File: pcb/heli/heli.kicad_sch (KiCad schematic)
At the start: 34 parts, among them J1 Batterie, J2 Debug, J3 Radio, J4 Servo, J5 Servo, Q1 IRLZ44N, SW1 SW_MEC_5E, U1 AZ1117-3.3, U2 MPU-6050, U3 STM32F103CBTx, Y1 8MHz

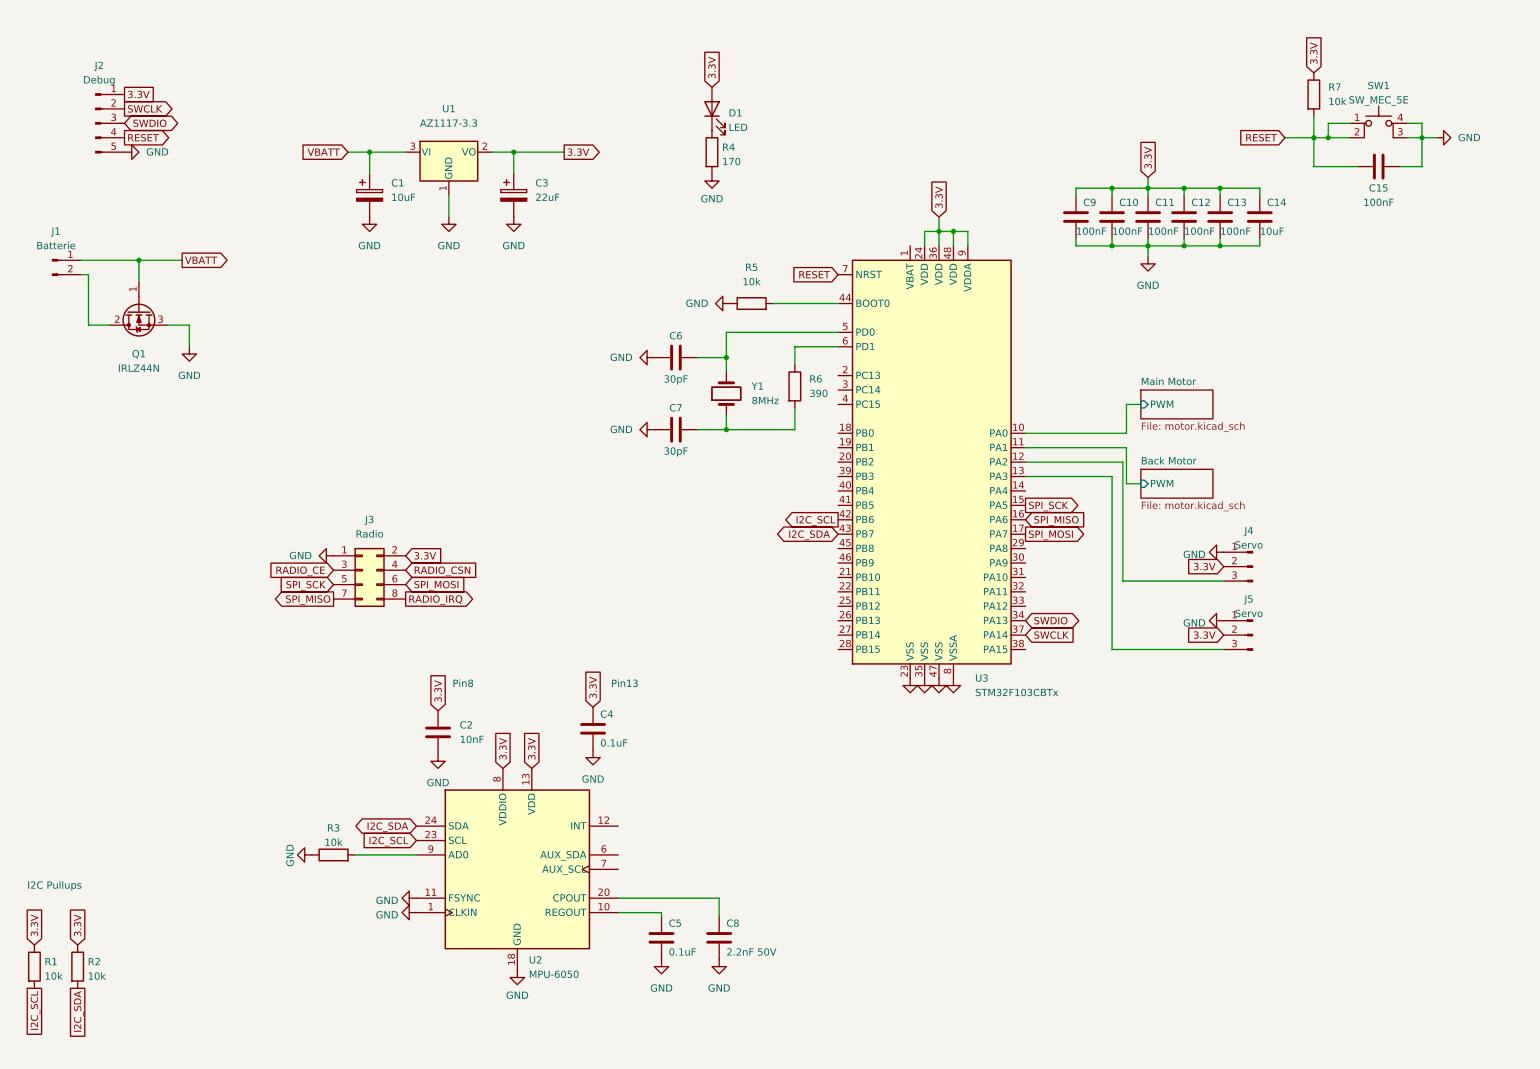
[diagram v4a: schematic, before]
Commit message: 
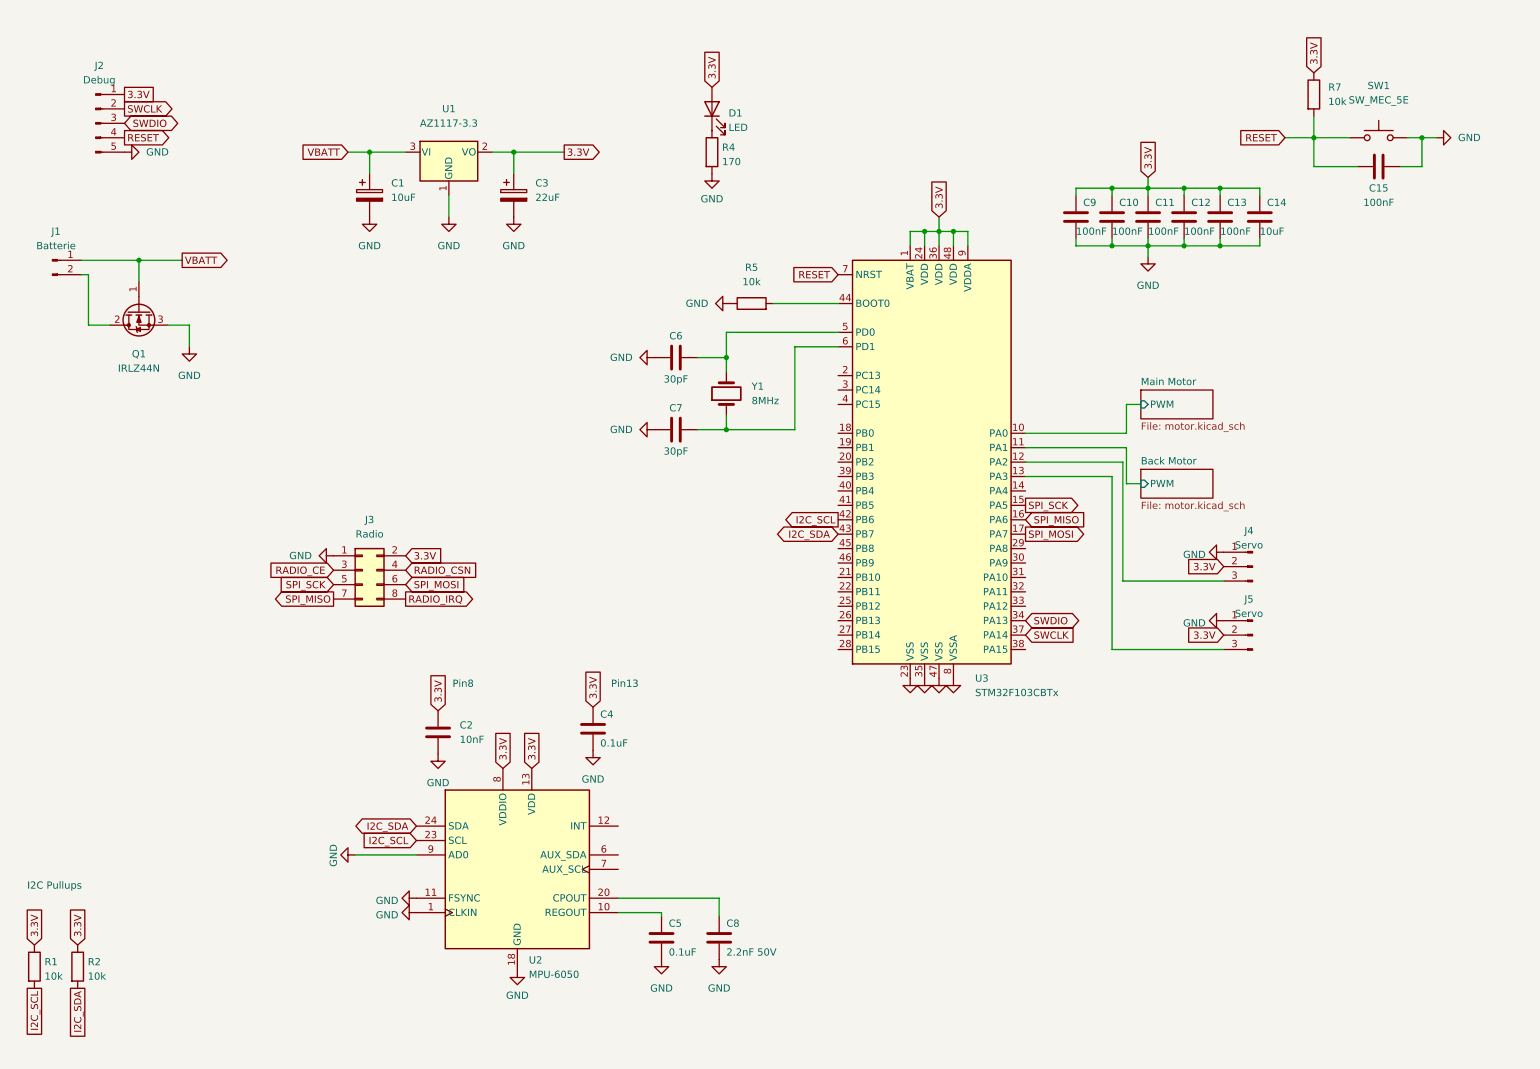
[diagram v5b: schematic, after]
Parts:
- removed R3: 10k, Resistor_SMD:R_0603_1608Metric, symbol Device:R
- removed R6: 390, Resistor_SMD:R_0603_1608Metric, symbol Device:R
- SW1: symbol Switch:SW_MEC_5E -> Switch:SW_Push
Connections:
- net 3.3V: now also U3.1 (VBAT)
- net GND: now also SW1.2, U2.9 (AD0); no longer SW1.3 (K), SW1.4 (A)
- net RESET: no longer SW1.2
- net at C7.2, Y1.1: now also U3.6 (PD1)
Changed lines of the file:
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@@
   (junction (at 245.11 34.29) (diameter 0) (color 0 0 0 0)
   )
-  (junction (at 247.65 34.29) (diameter 0) (color 0 0 0 0)
-  )
   (junction (at 222.25 43.18) (diameter 0) (color 0 0 0 0)
   )
@@
   (junction (at 215.9 43.18) (diameter 0) (color 0 0 0 0)
   )
+  (junction (at 176.53 50.8) (diameter 0) (color 0 0 0 0)
+  )
   (wire (pts (xy 136.525 85.725) (xy 141.605 85.725))
     (stroke (width 0) (type default) (color 0 0 0 0))
@@
     (stroke (width 0) (type default) (color 0 0 0 0))
   )
-  (wire (pts (xy 247.65 31.75) (xy 251.46 31.75))
-    (stroke (width 0) (type default) (color 0 0 0 0))
-  )
   (wire (pts (xy 78.74 36.83) (xy 78.74 40.64))
     (stroke (width 0) (type default) (color 0 0 0 0))
@@
     (stroke (width 0) (type default) (color 0 0 0 0))
   )
-  (wire (pts (xy 245.11 34.29) (xy 247.65 34.29))
-    (stroke (width 0) (type default) (color 0 0 0 0))
-  )
   (wire (pts (xy 209.55 43.18) (xy 215.9 43.18))
     (stroke (width 0) (type default) (color 0 0 0 0))
@@
     (stroke (width 0) (type default) (color 0 0 0 0))
   )
+  (wire (pts (xy 173.99 50.8) (xy 173.99 53.34))
+    (stroke (width 0) (type default) (color 0 0 0 0))
+  )
   (wire (pts (xy 264.16 34.29) (xy 266.7 34.29))
     (stroke (width 0) (type default) (color 0 0 0 0))
@@
     (stroke (width 0) (type default) (color 0 0 0 0))
   )
-  (wire (pts (xy 153.67 81.915) (xy 153.67 85.725))
-    (stroke (width 0) (type default) (color 0 0 0 0))
-  )
-  (wire (pts (xy 153.67 71.12) (xy 153.67 74.295))
+  (wire (pts (xy 176.53 50.8) (xy 173.99 50.8))
+    (stroke (width 0) (type default) (color 0 0 0 0))
+  )
+  (wire (pts (xy 153.67 71.12) (xy 153.67 85.725))
     (stroke (width 0) (type default) (color 0 0 0 0))
   )
@@
     (stroke (width 0) (type default) (color 0 0 0 0))
   )
-  (wire (pts (xy 247.65 34.29) (xy 247.65 31.75))
-    (stroke (width 0) (type default) (color 0 0 0 0))
-  )
-  (wire (pts (xy 247.65 34.29) (xy 251.46 34.29))
+  (wire (pts (xy 245.11 34.29) (xy 251.46 34.29))
     (stroke (width 0) (type default) (color 0 0 0 0))
   )
@@
   )
   (wire (pts (xy 261.62 34.29) (xy 264.16 34.29))
-    (stroke (width 0) (type default) (color 0 0 0 0))
-  )
-  (wire (pts (xy 261.62 31.75) (xy 264.16 31.75))
-    (stroke (width 0) (type default) (color 0 0 0 0))
-  )
-  (wire (pts (xy 264.16 31.75) (xy 264.16 34.29))
     (stroke (width 0) (type default) (color 0 0 0 0))
   )
@@
     (pin "2")
   )
-  (symbol (lib_id "power:GND") (at 68.58 160.655 270) (unit 1)
+  (symbol (lib_id "power:GND") (at 76.2 160.655 270) (unit 1)
     (in_bom yes) (on_board yes)
-    (property "Reference" "#PWR03" (id 0) (at 62.23 160.655 0)
-      (effects (font (size 1.27 1.27)) hide)
-    )
-    (property "Value" "GND" (id 1) (at 64.77 158.75 0)
-      (effects (font (size 1.27 1.27)) (justify left))
-    )
-    (property "Footprint" "" (id 2) (at 68.58 160.655 0)
-      (effects (font (size 1.27 1.27)) hide)
-    )
-    (property "Datasheet" "" (id 3) (at 68.58 160.655 0)
+    (property "Reference" "#PWR03" (id 0) (at 69.85 160.655 0)
+      (effects (font (size 1.27 1.27)) hide)
+    )
+    (property "Value" "GND" (id 1) (at 72.39 158.75 0)
+      (effects (font (size 1.27 1.27)) (justify left))
+    )
+    (property "Footprint" "" (id 2) (at 76.2 160.655 0)
+      (effects (font (size 1.27 1.27)) hide)
+    )
+    (property "Datasheet" "" (id 3) (at 76.2 160.655 0)
       (effects (font (size 1.27 1.27)) hide)
     )
@@
     (pin "2")
   )
-  (symbol (lib_id "Device:R") (at 153.67 78.105 0) (unit 1)
-    (in_bom yes) (on_board yes) (fields_autoplaced)
-    (property "Reference" "R6" (id 0) (at 156.21 76.8349 0)
-      (effects (font (size 1.27 1.27)) (justify left))
-    )
-    (property "Value" "390" (id 1) (at 156.21 79.3749 0)
-      (effects (font (size 1.27 1.27)) (justify left))
-    )
-    (property "Footprint" "Resistor_SMD:R_0603_1608Metric" (id 2) (at 151.892 78.105 90)
-      (effects (font (size 1.27 1.27)) hide)
-    )
-    (property "Datasheet" "~" (id 3) (at 153.67 78.105 0)
-      (effects (font (size 1.27 1.27)) hide)
-    )
-    (pin "1")
-    (pin "2")
-  )
   (symbol (lib_id "power:GND") (at 142.24 63.5 270) (unit 1)
     (in_bom yes) (on_board yes) (fields_autoplaced)
@@
     (pin "1")
   )
-  (symbol (lib_id "Switch:SW_MEC_5E") (at 256.54 34.29 0) (unit 1)
+  (symbol (lib_id "Switch:SW_Push") (at 256.54 34.29 0) (unit 1)
     (in_bom yes) (on_board yes) (fields_autoplaced)
     (property "Reference" "SW1" (id 0) (at 256.54 25.1292 0))
     (property "Value" "SW_MEC_5E" (id 1) (at 256.54 27.6661 0))
-    (property "Footprint" "Button_Switch_SMD:SW_SPST_TL3305A" (id 2) (at 256.54 26.67 0)
-      (effects (font (size 1.27 1.27)) hide)
-    )
-    (property "Datasheet" "http://www.apem.com/int/index.php?controller=attachment&id_attachment=1371" (id 3) (at 256.54 26.67 0)
-      (effects (font (size 1.27 1.27)) hide)
-    )
-    (pin "1")
-    (pin "2")
-    (pin "3")
-    (pin "4")
+    (property "Footprint" "Button_Switch_SMD:SW_SPST_TL3305A" (id 2) (at 256.54 29.21 0)
+      (effects (font (size 1.27 1.27)) hide)
+    )
+    (property "Datasheet" "~" (id 3) (at 256.54 29.21 0)
+      (effects (font (size 1.27 1.27)) hide)
+    )
+    (pin "1")
+    (pin "2")
   )
   (symbol (lib_id "Device:LED") (at 139.065 29.21 90) (unit 1)
@@
     )
     (pin "1")
-  )
-  (symbol (lib_id "Device:R") (at 72.39 160.655 90) (unit 1)
-    (in_bom yes) (on_board yes) (fields_autoplaced)
-    (property "Reference" "R3" (id 0) (at 72.39 155.9392 90))
-    (property "Value" "10k" (id 1) (at 72.39 158.4761 90))
-    (property "Footprint" "Resistor_SMD:R_0603_1608Metric" (id 2) (at 72.39 162.433 90)
-      (effects (font (size 1.27 1.27)) hide)
-    )
-    (property "Datasheet" "~" (id 3) (at 72.39 160.655 0)
-      (effects (font (size 1.27 1.27)) hide)
-    )
-    (pin "1")
-    (pin "2")
   )
   (symbol (lib_id "Device:R") (at 27.305 180.34 0) (unit 1)
@@
       (reference "R2") (unit 1) (value "10k") (footprint "Resistor_SMD:R_0603_1608Metric")
     )
-    (path "/cc0ffb09-4eb8-433b-b264-45e95fc87cf9"
-      (reference "R3") (unit 1) (value "10k") (footprint "Resistor_SMD:R_0603_1608Metric")
-    )
     (path "/e5d85d82-5fcc-4bcc-b9ab-9d364f5d09a5"
       (reference "R4") (unit 1) (value "170") (footprint "Resistor_SMD:R_0603_1608Metric")
@@
       (reference "R5") (unit 1) (value "10k") (footprint "Resistor_SMD:R_0603_1608Metric")
     )
-    (path "/6d581789-cce3-4f83-aa35-511d58ddc4ad"
-      (reference "R6") (unit 1) (value "390") (footprint "Resistor_SMD:R_0603_1608Metric")
-    )
     (path "/07b9ea31-e11e-4458-853a-674533568a29"

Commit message: 
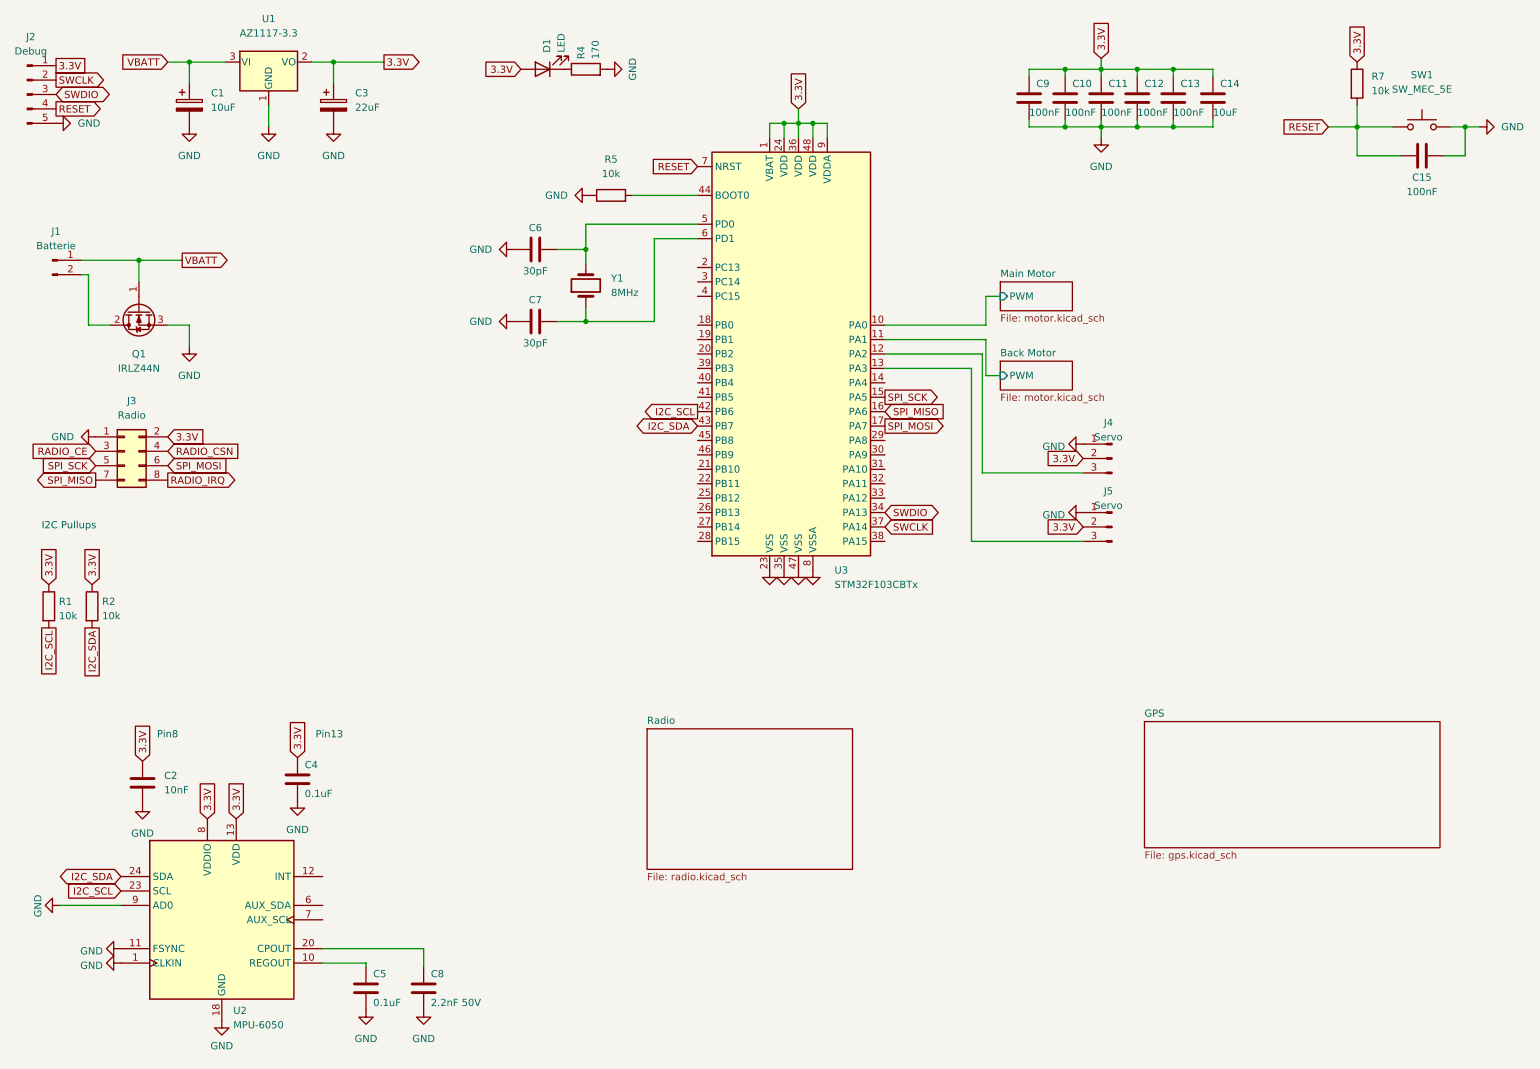
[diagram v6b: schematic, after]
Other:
- added sheet GPS (gps.kicad_sch)
- added sheet Radio (radio.kicad_sch)
- moved on the sheet: C1, C10, C11, C12, C13, C14, C15, C2, C3, C4, C5, C6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
